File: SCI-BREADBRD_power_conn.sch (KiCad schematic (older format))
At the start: 2 parts

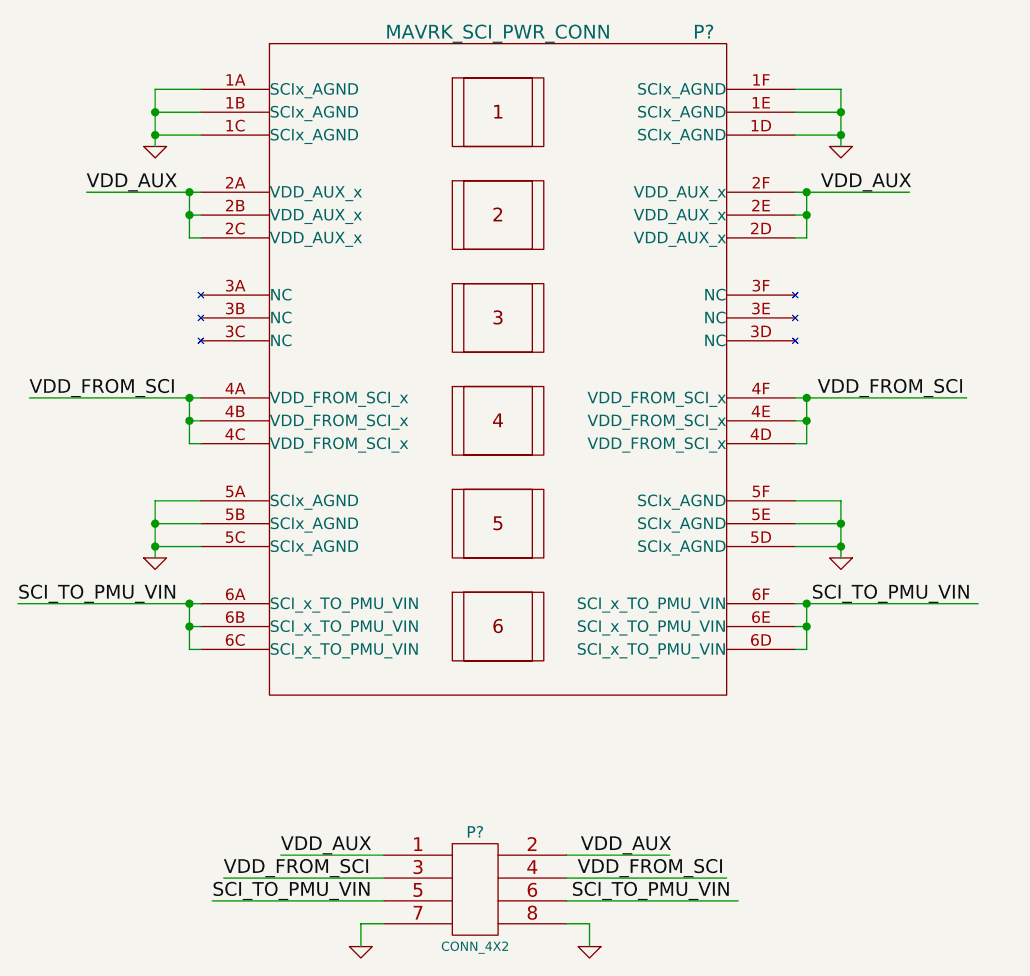
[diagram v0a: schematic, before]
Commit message: Fixed the footprint properties of various parts throughout the schematic to make sure they are all point to valid footprints.
Added SCI-BREADBRD.cmp to specify which footprints should be used for
each part.

Added netlists to the .gitignore as those can be generated easily in
eeschema.
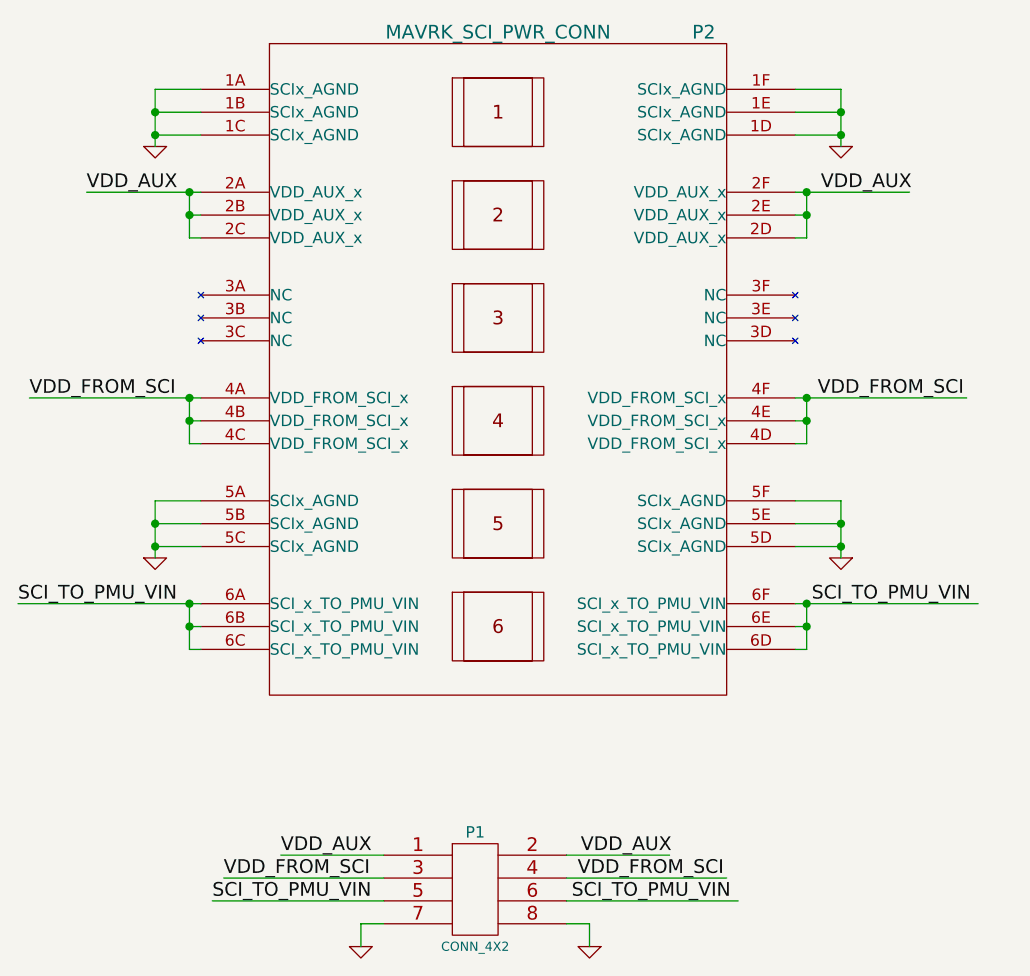
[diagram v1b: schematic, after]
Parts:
- P1: renamed from P?; footprint PIN_ARRAY_2x4 -> pin_array_4x2
- P2: renamed from P?; footprint UPT-06-03_0-01-L-V -> SAMTEC_UPT-06-03_0-01-L-V
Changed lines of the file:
@@
-EESchema Schematic File Version 2  date Fri 27 Apr 2012 04:22:34 AM EDT
+EESchema Schematic File Version 2  date Fri 27 Apr 2012 08:55:37 AM EDT
 LIBS:custom_transistors
 LIBS:TI_custom
@@
 $EndDescr
 $Comp
-L MAVRK_SCI_PWR_CONN P?
+L MAVRK_SCI_PWR_CONN P2
 U 1 1 4F9A6200
 P 5750 2950
-F 0 "P?" H 6650 4400 60  0000 C CNN
+F 0 "P2" H 6650 4400 60  0000 C CNN
 F 1 "MAVRK_SCI_PWR_CONN" H 5750 4400 60  0000 C CNN
-F 2 "UPT-06-03_0-01-L-V" H 5750 2950 60  0001 C CNN
+F 2 "SAMTEC_UPT-06-03_0-01-L-V" H 5750 2950 60  0001 C CNN
 F 4 "Samtec" H 5750 2950 60  0001 C CNN "Manufacturer"
 F 5 "UPT-06-03.0-01-L-V" H 5750 2950 60  0001 C CNN "Part Number"
@@
 $EndComp
 $Comp
-L GND #PWR?
+L GND #PWR01
 U 1 1 4F9A6206
 P 4250 2000
-F 0 "#PWR?" H 4250 2000 30  0001 C CNN
+F 0 "#PWR01" H 4250 2000 30  0001 C CNN
 F 1 "GND" H 4250 1930 30  0001 C CNN
 	1    4250 2000
@@
 $EndComp
 $Comp
-L GND #PWR?
+L GND #PWR02
 U 1 1 4F9A620C
 P 7250 2000
-F 0 "#PWR?" H 7250 2000 30  0001 C CNN
+F 0 "#PWR02" H 7250 2000 30  0001 C CNN
 F 1 "GND" H 7250 1930 30  0001 C CNN
 	1    7250 2000
@@
 $EndComp
 $Comp
-L GND #PWR?
+L GND #PWR03
 U 1 1 4F9A6212
 P 4250 3800
-F 0 "#PWR?" H 4250 3800 30  0001 C CNN
+F 0 "#PWR03" H 4250 3800 30  0001 C CNN
 F 1 "GND" H 4250 3730 30  0001 C CNN
 	1    4250 3800
@@
 $EndComp
 $Comp
-L GND #PWR?
+L GND #PWR04
 U 1 1 4F9A6218
 P 7250 3800
-F 0 "#PWR?" H 7250 3800 30  0001 C CNN
+F 0 "#PWR04" H 7250 3800 30  0001 C CNN
 F 1 "GND" H 7250 3730 30  0001 C CNN
 	1    7250 3800
@@
 SCI_TO_PMU_VIN
 $Comp
-L CONN_4X2 P?
+L CONN_4X2 P1
 U 1 1 4F9A622A
 P 5650 5250
-F 0 "P?" H 5650 5500 50  0000 C CNN
+F 0 "P1" H 5650 5500 50  0000 C CNN
 F 1 "CONN_4X2" H 5650 5000 40  0000 C CNN
-F 2 "PIN_ARRAY_2x4" H 5650 5250 60  0001 C CNN
+F 2 "pin_array_4x2" H 5650 5250 60  0001 C CNN
 F 4 "TE Connectivity" H 5650 5250 60  0001 C CNN "Manufacturer"
 F 5 "5-534206-4" H 5650 5250 60  0001 C CNN "Part Number"
@@
 $EndComp
 $Comp
-L GND #PWR?
+L GND #PWR05
 U 1 1 4F9A6230
 P 5150 5500
-F 0 "#PWR?" H 5150 5500 30  0001 C CNN
+F 0 "#PWR05" H 5150 5500 30  0001 C CNN
 F 1 "GND" H 5150 5430 30  0001 C CNN
 	1    5150 5500
@@
 SCI_TO_PMU_VIN
 $Comp
-L GND #PWR?
+L GND #PWR06
 U 1 1 4F9A6239
 P 6150 5500
-F 0 "#PWR?" H 6150 5500 30  0001 C CNN
+F 0 "#PWR06" H 6150 5500 30  0001 C CNN
 F 1 "GND" H 6150 5430 30  0001 C CNN
 	1    6150 5500
